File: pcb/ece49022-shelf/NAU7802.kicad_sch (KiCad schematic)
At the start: 10 parts, among them IC1 NAU7802

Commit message: added footprints
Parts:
- C1, C3, C4: footprint (none) -> 49022_Footprints:C_0402_1005Metric_small_pads
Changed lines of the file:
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@@
 			)
 		)
-		(property "Footprint" ""
+		(property "Footprint" "49022_Footprints:C_0402_1005Metric_small_pads"
 			(at 172.72 125.73 0)
 			(effects
@@
 			)
 		)
-		(property "Footprint" ""
+		(property "Footprint" "49022_Footprints:C_0402_1005Metric_small_pads"
 			(at 165.1 113.03 0)
 			(effects
@@
 			)
 		)
-		(property "Footprint" ""
+		(property "Footprint" "49022_Footprints:C_0402_1005Metric_small_pads"
 			(at 180.34 125.73 0)
 			(effects

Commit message: updated footprints, pcb
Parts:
- C2, C5: footprint (none) -> Capacitor_SMD:C_0402_1005Metric
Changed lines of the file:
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@@
 			)
 		)
-		(property "Footprint" ""
+		(property "Footprint" "Capacitor_SMD:C_0402_1005Metric"
 			(at 129.54 90.17 0)
 			(effects
@@
 		(dnp no)
 		(fields_autoplaced yes)
-		(property "Reference" "#PWR021"
+		(property "Reference" "#PWR0101"
 			(at 180.34 138.43 0)
 			(effects
@@
 			(project "ece49022-shelf"
 				(path "/cb6cb1b4-c151-4aa2-8cd7-5430288cfa02/fb213d7f-28bb-4d6d-ba03-4017b4d07db5"
-					(reference "#PWR021")
+					(reference "#PWR0101")
 					(unit 1)
 				)
@@
 		(dnp no)
 		(fields_autoplaced yes)
-		(property "Reference" "#PWR022"
+		(property "Reference" "#PWR0104"
 			(at 217.17 109.22 0)
 			(effects
@@
 			(project "ece49022-shelf"
 				(path "/cb6cb1b4-c151-4aa2-8cd7-5430288cfa02/fb213d7f-28bb-4d6d-ba03-4017b4d07db5"
-					(reference "#PWR022")
+					(reference "#PWR0104")
 					(unit 1)
 				)
@@
 			)
 		)
-		(property "Footprint" ""
+		(property "Footprint" "Capacitor_SMD:C_0402_1005Metric"
 			(at 168.91 102.87 0)
 			(effects
@@
 		(dnp no)
 		(fields_autoplaced yes)
-		(property "Reference" "#PWR017"
+		(property "Reference" "#PWR0103"
 			(at 132.08 138.43 0)
 			(effects
@@
 			(project "ece49022-shelf"
 				(path "/cb6cb1b4-c151-4aa2-8cd7-5430288cfa02/fb213d7f-28bb-4d6d-ba03-4017b4d07db5"
-					(reference "#PWR017")
+					(reference "#PWR0103")
 					(unit 1)
 				)
@@
 		(dnp no)
 		(fields_autoplaced yes)
-		(property "Reference" "#PWR019"
+		(property "Reference" "#PWR0102"
 			(at 165.1 138.43 0)
 			(effects
@@
 			(project "ece49022-shelf"
 				(path "/cb6cb1b4-c151-4aa2-8cd7-5430288cfa02/fb213d7f-28bb-4d6d-ba03-4017b4d07db5"
-					(reference "#PWR019")
-					(unit 1)
-				)
+					(reference "#PWR0102")
+					(unit 1)
+				)

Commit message: Started Layout
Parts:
- added C32, C6: 0.1uF, 25V, Capacitor_SMD:C_0402_1005Metric, symbol Device:C_Small
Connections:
- net AVDD: now also C6.1
- net GND: now also C32.2, C6.2
- net VCC: now also C32.1

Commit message: working n board
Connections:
- net VCC is gone; now on net +5V: C32.1, IC1.15 (DVDD), R3.2, R4.2
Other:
- moved on the sheet: C32
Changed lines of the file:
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@@
 	(wire
 		(pts
-			(xy 147.32 82.55) (xy 147.32 87.63)
+			(xy 147.32 82.55) (xy 147.32 83.82)
 		)
 		(stroke
@@
 	(wire
 		(pts
-			(xy 147.32 92.71) (xy 147.32 93.98)
+			(xy 147.32 88.9) (xy 147.32 90.17)
 		)
 		(stroke
@@
 	(symbol
 		(lib_id "power:GND")
-		(at 147.32 93.98 0)
+		(at 147.32 90.17 0)
 		(unit 1)
 		(exclude_from_sim no)
@@
 		(dnp no)
 		(property "Reference" "#PWR056"
-			(at 147.32 100.33 0)
+			(at 147.32 96.52 0)
 			(effects
 				(font
@@
 		)
 		(property "Value" "GND"
-			(at 147.32 98.298 0)
+			(at 147.32 94.488 0)
 			(effects
 				(font
@@
 		)
 		(property "Footprint" ""
-			(at 147.32 93.98 0)
+			(at 147.32 90.17 0)
 			(effects
 				(font
@@
 		)
 		(property "Datasheet" ""
-			(at 147.32 93.98 0)
+			(at 147.32 90.17 0)
 			(effects
 				(font
@@
 		)
 		(property "Description" "Power symbol creates a global label with name \"GND\" , ground"
-			(at 147.32 93.98 0)
+			(at 147.32 90.17 0)
 			(effects
 				(font
@@
 				(path "/cb6cb1b4-c151-4aa2-8cd7-5430288cfa02/fb213d7f-28bb-4d6d-ba03-4017b4d07db5"
 					(reference "#PWR056")
-					(unit 1)
-				)
-			)
-		)
-	)
-	(symbol
-		(lib_id "NAU7802-eagle-import:VCC")
-		(at 109.22 81.28 0)
-		(unit 1)
-		(exclude_from_sim no)
-		(in_bom yes)
-		(on_board yes)
-		(dnp no)
-		(property "Reference" "#P+2"
-			(at 109.22 81.28 0)
-			(effects
-				(font
-					(size 1.27 1.27)
-				)
-				(hide yes)
-			)
-		)
-		(property "Value" "VCC"
-			(at 106.68 83.82 90)
-			(effects
-				(font
-					(size 1.778 1.5113)
-				)
-				(justify left bottom)
-			)
-		)
-		(property "Footprint" ""
-			(at 109.22 81.28 0)
-			(effects
-				(font
-					(size 1.27 1.27)
-				)
-				(hide yes)
-			)
-		)
-		(property "Datasheet" ""
-			(at 109.22 81.28 0)
-			(effects
-				(font
-					(size 1.27 1.27)
-				)
-				(hide yes)
-			)
-		)
-		(property "Description" ""
-			(at 109.22 81.28 0)
-			(effects
-				(font
-					(size 1.27 1.27)
-				)
-				(hide yes)
-			)
-		)
-		(pin "1"
-		)
-		(instances
-			(project ""
-				(path "/cb6cb1b4-c151-4aa2-8cd7-5430288cfa02/fb213d7f-28bb-4d6d-ba03-4017b4d07db5"
-					(reference "#P+2")
-					(unit 1)
-				)
-			)
-			(project ""
-				(path "/f46caa08-94e3-4c42-8462-81738f26da11"
-					(reference "#P+2")
 					(unit 1)
 				)
@@
 				(path "/cb6cb1b4-c151-4aa2-8cd7-5430288cfa02/fb213d7f-28bb-4d6d-ba03-4017b4d07db5"
 					(reference "#U$01")
+					(unit 1)
+				)
+			)
+		)
+	)
+	(symbol
+		(lib_id "power:+5V")
+		(at 109.22 83.82 0)
+		(unit 1)
+		(exclude_from_sim no)
+		(in_bom yes)
+		(on_board yes)
+		(dnp no)
+		(fields_autoplaced yes)
+		(property "Reference" "#PWR057"
+			(at 109.22 87.63 0)
+			(effects
+				(font
+					(size 1.27 1.27)
+				)
+				(hide yes)
+			)
+		)
+		(property "Value" "+5V"
+			(at 109.22 78.74 0)
+			(effects
+				(font
+					(size 1.27 1.27)
+				)
+			)
+		)
+		(property "Footprint" ""
+			(at 109.22 83.82 0)
+			(effects
+				(font
+					(size 1.27 1.27)
+				)
+				(hide yes)
+			)
+		)
+		(property "Datasheet" ""
+			(at 109.22 83.82 0)
+			(effects
+				(font
+					(size 1.27 1.27)
+				)
+				(hide yes)
+			)
+		)
+		(property "Description" "Power symbol creates a global label with name \"+5V\""
+			(at 109.22 83.82 0)
+			(effects
+				(font
+					(size 1.27 1.27)
+				)
+				(hide yes)
+			)
+		)
+		(pin "1"
+		)
+		(instances
+			(project "ece49022-shelf"
+				(path "/cb6cb1b4-c151-4aa2-8cd7-5430288cfa02/fb213d7f-28bb-4d6d-ba03-4017b4d07db5"
+					(reference "#PWR057")
 					(unit 1)
 				)
@@
 		)
 		(property "Value" "0.1uF, 25V"
-			(at 136.906 68.834 0)
+			(at 131.064 75.946 0)
 			(effects
 				(font
@@
 	)
 	(symbol
-		(lib_id "NAU7802-eagle-import:VCC")
-		(at 147.32 76.2 0)
-		(mirror y)
-		(unit 1)
-		(exclude_from_sim no)
-		(in_bom yes)
-		(on_board yes)
-		(dnp no)
-		(property "Reference" "#P+7"
-			(at 147.32 76.2 0)
-			(effects
-				(font
-					(size 1.27 1.27)
-				)
-				(hide yes)
-			)
-		)
-		(property "Value" "VCC"
-			(at 149.86 78.74 90)
-			(effects
-				(font
-					(size 1.778 1.5113)
-				)
-				(justify left bottom)
-			)
-		)
-		(property "Footprint" ""
-			(at 147.32 76.2 0)
-			(effects
-				(font
-					(size 1.27 1.27)
-				)
-				(hide yes)
-			)
-		)
-		(property "Datasheet" ""
-			(at 147.32 76.2 0)
-			(effects
-				(font
-					(size 1.27 1.27)
-				)
-				(hide yes)
-			)
-		)
-		(property "Description" ""
-			(at 147.32 76.2 0)
-			(effects
-				(font
-					(size 1.27 1.27)
-				)
-				(hide yes)
-			)
-		)
-		(pin "1"
-		)
-		(instances
-			(project ""
-				(path "/cb6cb1b4-c151-4aa2-8cd7-5430288cfa02/fb213d7f-28bb-4d6d-ba03-4017b4d07db5"
-					(reference "#P+7")
-					(unit 1)
-				)
-			)
-			(project ""
-				(path "/f46caa08-94e3-4c42-8462-81738f26da11"
-					(reference "#P+7")
-					(unit 1)
-				)
-			)
-		)
-	)
-	(symbol
 		(lib_id "Device:C_Small")
 		(at 168.91 102.87 0)
@@
 		(dnp no)
 		(property "Reference" "IC1"
-			(at 152.4 96.52 0)
+			(at 154.94 96.266 0)
 			(effects
 				(font
@@
 	(symbol
 		(lib_id "Device:C_Small")
-		(at 147.32 90.17 0)
+		(at 147.32 86.36 0)
 		(unit 1)
 		(exclude_from_sim no)
@@
 		(dnp no)
 		(property "Reference" "C32"
-			(at 149.352 90.17 0)
+			(at 149.352 86.36 0)
 			(effects
 				(font
@@
 		)
 		(property "Value" "0.1uF, 25V"
-			(at 148.336 88.138 0)
+			(at 148.336 84.328 0)
 			(effects
 				(font
@@
 		)
 		(property "Footprint" "Capacitor_SMD:C_0402_1005Metric"
-			(at 147.32 90.17 0)
+			(at 147.32 86.36 0)
 			(effects
 				(font
@@
 		)
 		(property "Datasheet" "~"
-			(at 147.32 90.17 0)
+			(at 147.32 86.36 0)
 			(effects
 				(font
@@
 		)
 		(property "Description" "0402B104K250HI"
-			(at 147.32 90.17 0)
+			(at 147.32 86.36 0)
 			(effects
 				(font
@@
 					(unit 1)
 				)
+			)
+		)
+	)
+	(symbol
+		(lib_id "power:+5V")
+		(at 147.32 78.74 0)
+		(unit 1)
+		(exclude_from_sim no)
+		(in_bom yes)
+		(on_board yes)
+		(dnp no)
+		(fields_autoplaced yes)
+		(property "Reference" "#PWR058"
+			(at 147.32 82.55 0)
+			(effects
+				(font
+					(size 1.27 1.27)
+				)
+				(hide yes)
+			)
+		)
+		(property "Value" "+5V"
+			(at 147.32 73.66 0)
+			(effects
+				(font
+					(size 1.27 1.27)
+				)
+			)
+		)
+		(property "Footprint" ""
+			(at 147.32 78.74 0)
+			(effects
+				(font
+					(size 1.27 1.27)
+				)
+				(hide yes)
+			)
+		)
+		(property "Datasheet" ""
+			(at 147.32 78.74 0)
+			(effects
+				(font
+					(size 1.27 1.27)
+				)
+				(hide yes)
+			)
+		)
+		(property "Description" "Power symbol creates a global label with name \"+5V\""
+			(at 147.32 78.74 0)
+			(effects
+				(font
+					(size 1.27 1.27)
+				)
+				(hide yes)
+			)
+		)
+		(pin "1"
+		)
+		(instances
+			(project "ece49022-shelf"
+				(path "/cb6cb1b4-c151-4aa2-8cd7-5430288cfa02/fb213d7f-28bb-4d6d-ba03-4017b4d07db5"
+					(reference "#PWR058")
+					(unit 1)
+				)

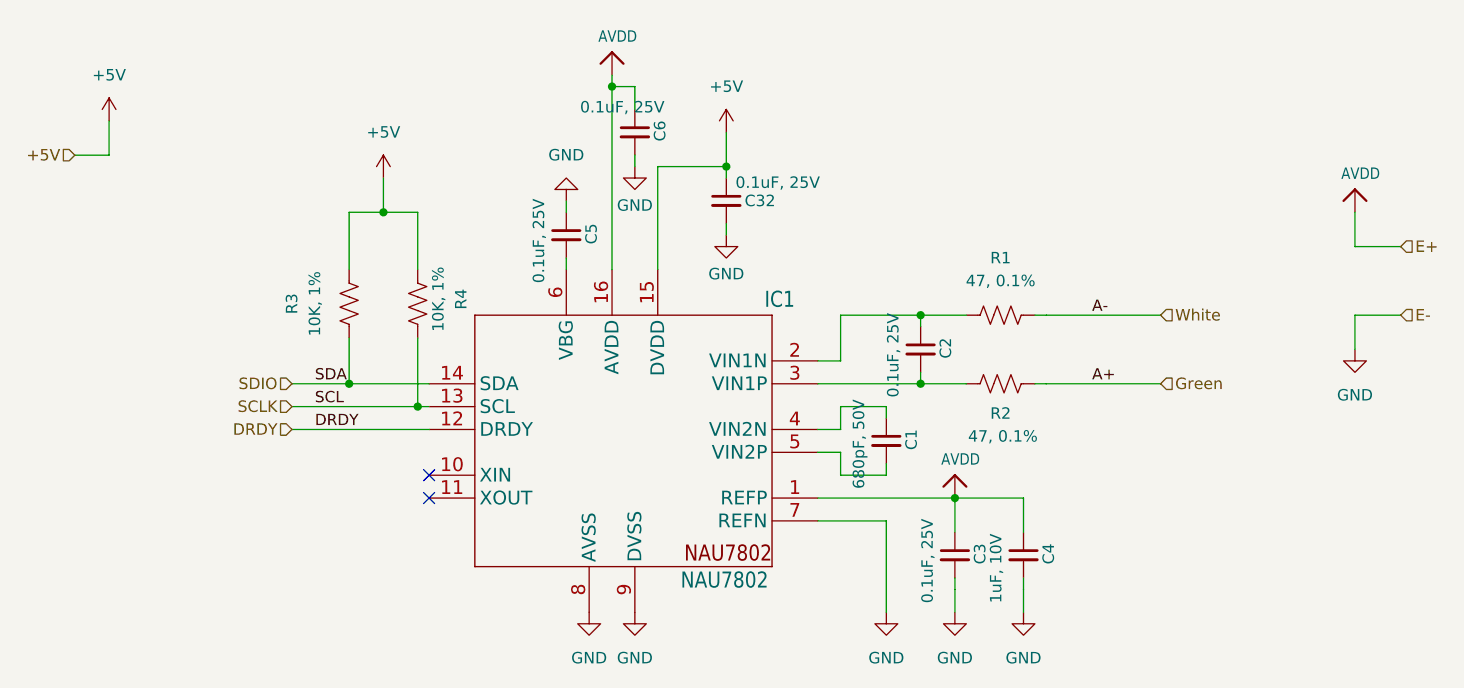
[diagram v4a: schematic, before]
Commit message: update footprint and part selection
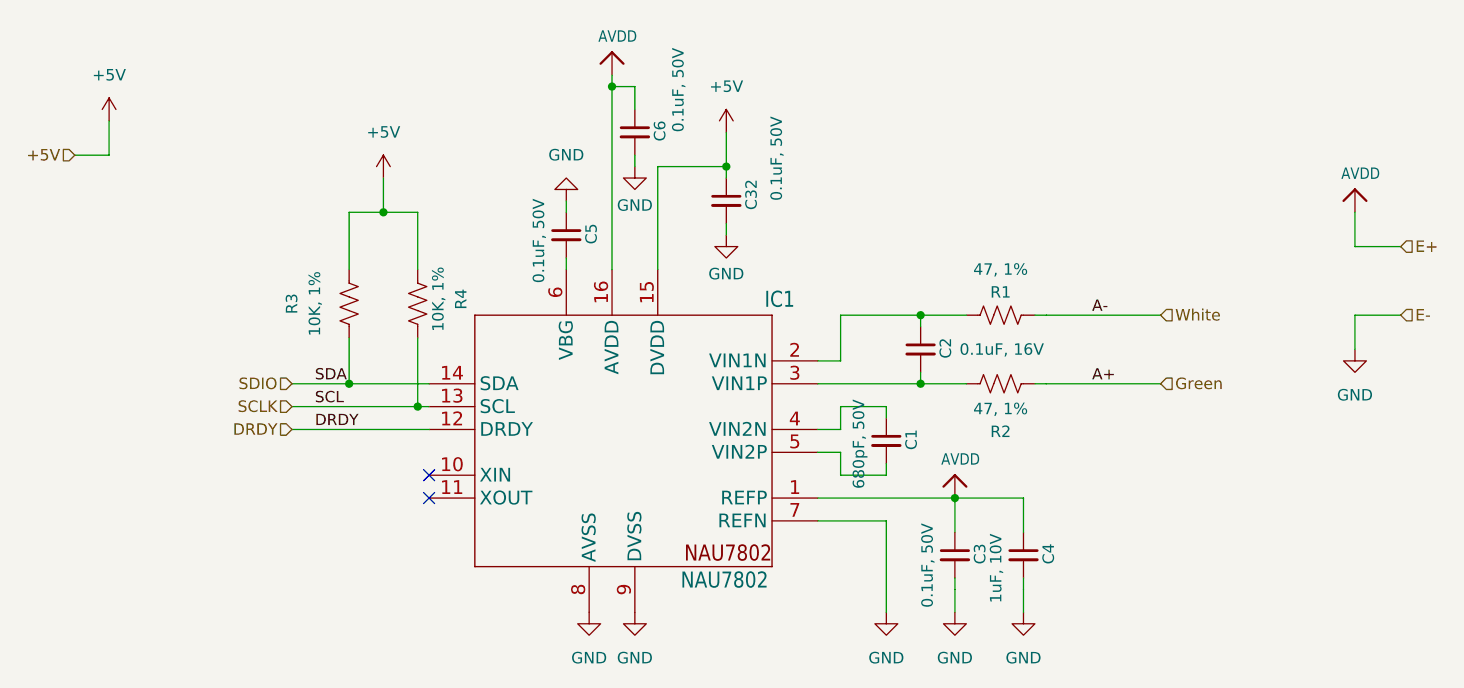
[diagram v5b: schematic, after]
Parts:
- C1, C4: footprint 49022_Footprints:C_0402_1005Metric_small_pads -> Capacitor_SMD:C_0402_1005Metric_Pad0.74x0.62mm_HandSolder
- C2: value 0.1uF, 25V -> 0.1uF, 16V; footprint Capacitor_SMD:C_0402_1005Metric -> Capacitor_SMD:C_0402_1005Metric_Pad0.74x0.62mm_HandSolder
- C3: value 0.1uF, 25V -> 0.1uF, 50V; footprint 49022_Footprints:C_0402_1005Metric_small_pads -> Capacitor_SMD:C_0402_1005Metric_Pad0.74x0.62mm_HandSolder
- C32, C5, C6: value 0.1uF, 25V -> 0.1uF, 50V; footprint Capacitor_SMD:C_0402_1005Metric -> Capacitor_SMD:C_0402_1005Metric_Pad0.74x0.62mm_HandSolder
- R1, R2: value 47, 0.1% -> 47, 1%

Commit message: edited nau7802 schem and changed pins for layout reasons
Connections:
- net +5V: no longer R3.2, R4.2
- new net: R3.2, R4.2
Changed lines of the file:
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@@
+	(wire
+		(pts
+			(xy 88.9 81.28) (xy 92.71 81.28)
+		)
+		(stroke
+			(width 0)
+			(type default)
+		)
+	)
 	(wire
 		(pts
@@
 			(width 0.1524)
 			(type solid)
+		)
+	)
+	(wire
+		(pts
+			(xy 92.71 77.47) (xy 92.71 81.28)
+		)
+		(stroke
+			(width 0)
+			(type default)
 		)
 	)
@@
 		(shape input)
 		(at 99.06 106.68 180)
+		(effects
+			(font
+				(size 1.27 1.27)
+			)
+			(justify right)
+		)
+	)
+	(hierarchical_label "+3V3"
+		(shape input)
+		(at 88.9 81.28 180)
 		(effects
 			(font
@@
 	)
 	(symbol
-		(lib_id "power:+5V")
-		(at 109.22 83.82 0)
-		(unit 1)
-		(exclude_from_sim no)
-		(in_bom yes)
-		(on_board yes)
-		(dnp no)
-		(fields_autoplaced yes)
-		(property "Reference" "#PWR057"
-			(at 109.22 87.63 0)
-			(effects
-				(font
-					(size 1.27 1.27)
-				)
-				(hide yes)
-			)
-		)
-		(property "Value" "+5V"
-			(at 109.22 78.74 0)
-			(effects
-				(font
-					(size 1.27 1.27)
-				)
-			)
-		)
-		(property "Footprint" ""
-			(at 109.22 83.82 0)
-			(effects
-				(font
-					(size 1.27 1.27)
-				)
-				(hide yes)
-			)
-		)
-		(property "Datasheet" ""
-			(at 109.22 83.82 0)
-			(effects
-				(font
-					(size 1.27 1.27)
-				)
-				(hide yes)
-			)
-		)
-		(property "Description" "Power symbol creates a global label with name \"+5V\""
-			(at 109.22 83.82 0)
-			(effects
-				(font
-					(size 1.27 1.27)
-				)
-				(hide yes)
-			)
-		)
-		(pin "1"
-		)
-		(instances
-			(project "ece49022-shelf"
-				(path "/cb6cb1b4-c151-4aa2-8cd7-5430288cfa02/fb213d7f-28bb-4d6d-ba03-4017b4d07db5"
-					(reference "#PWR057")
-					(unit 1)
-				)
-			)
-		)
-	)
-	(symbol
 		(lib_id "power:GND")
 		(at 129.54 86.36 180)
@@
 					(unit 1)
 				)
+			)
+		)
+	)
+	(symbol
+		(lib_id "power:+3V3")
+		(at 92.71 77.47 0)
+		(unit 1)
+		(exclude_from_sim no)
+		(in_bom yes)
+		(on_board yes)
+		(dnp no)
+		(fields_autoplaced yes)
+		(property "Reference" "#PWR01"
+			(at 92.71 81.28 0)
+			(effects
+				(font
+					(size 1.27 1.27)
+				)
+				(hide yes)
+			)
+		)
+		(property "Value" "+3V3"
+			(at 92.71 72.39 0)
+			(effects
+				(font
+					(size 1.27 1.27)
+				)
+			)
+		)
+		(property "Footprint" ""
+			(at 92.71 77.47 0)
+			(effects
+				(font
+					(size 1.27 1.27)
+				)
+				(hide yes)
+			)
+		)
+		(property "Datasheet" ""
+			(at 92.71 77.47 0)
+			(effects
+				(font
+					(size 1.27 1.27)
+				)
+				(hide yes)
+			)
+		)
+		(property "Description" "Power symbol creates a global label with name \"+3V3\""
+			(at 92.71 77.47 0)
+			(effects
+				(font
+					(size 1.27 1.27)
+				)
+				(hide yes)
+			)
+		)
+		(pin "1"
+		)
+		(instances
+			(project ""
+				(path "/cb6cb1b4-c151-4aa2-8cd7-5430288cfa02/fb213d7f-28bb-4d6d-ba03-4017b4d07db5"
+					(reference "#PWR01")
+					(unit 1)
+				)

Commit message: working on stuff
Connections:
- net +3V3: now also R3.2, R4.2
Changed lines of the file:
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@@
+	)
+	(symbol
+		(lib_id "power:+3V3")
+		(at 109.22 83.82 0)
+		(unit 1)
+		(exclude_from_sim no)
+		(in_bom yes)
+		(on_board yes)
+		(dnp no)
+		(fields_autoplaced yes)
+		(property "Reference" "#PWR03"
+			(at 109.22 87.63 0)
+			(effects
+				(font
+					(size 1.27 1.27)
+				)
+				(hide yes)
+			)
+		)
+		(property "Value" "+3V3"
+			(at 109.22 78.74 0)
+			(effects
+				(font
+					(size 1.27 1.27)
+				)
+			)
+		)
+		(property "Footprint" ""
+			(at 109.22 83.82 0)
+			(effects
+				(font
+					(size 1.27 1.27)
+				)
+				(hide yes)
+			)
+		)
+		(property "Datasheet" ""
+			(at 109.22 83.82 0)
+			(effects
+				(font
+					(size 1.27 1.27)
+				)
+				(hide yes)
+			)
+		)
+		(property "Description" "Power symbol creates a global label with name \"+3V3\""
+			(at 109.22 83.82 0)
+			(effects
+				(font
+					(size 1.27 1.27)
+				)
+				(hide yes)
+			)
+		)
+		(pin "1"
+		)
+		(instances
+			(project "ece49022-shelf"
+				(path "/cb6cb1b4-c151-4aa2-8cd7-5430288cfa02/fb213d7f-28bb-4d6d-ba03-4017b4d07db5"
+					(reference "#PWR03")
+					(unit 1)
+				)
+			)
+		)
 	)
 	(symbol
